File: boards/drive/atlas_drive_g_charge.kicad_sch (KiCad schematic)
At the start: 50 parts, among them J701 USB_C_16P, J702 EEPROM_PROG, U701 TPS25751D, U702 M24512, U703 BQ25798

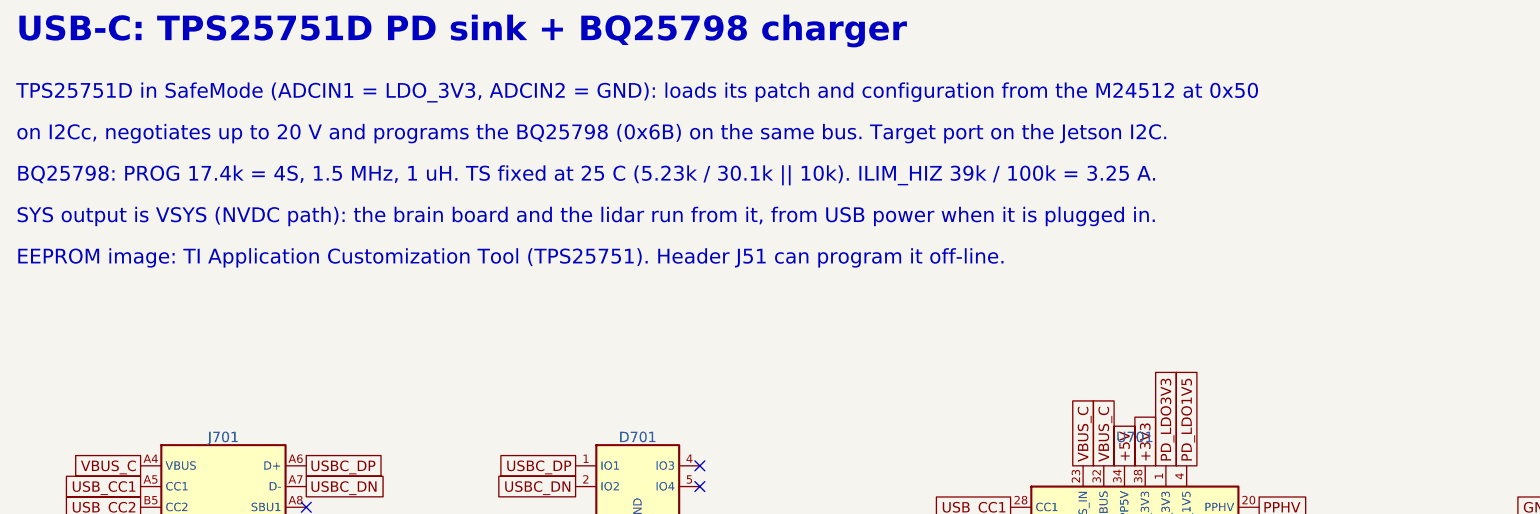
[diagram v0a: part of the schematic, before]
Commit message: Review fixes: docs, run_kicad.sh and drive board text
- README, docs/ARCHITECTURE.md, share/README.md, boards/tools/README.md: status,
  rebuild steps and tool notes brought up to date
- run_kicad.sh: the optional first argument is a sync tarball or an empty string
- Drive schematic text: header J702, 7.5 V servo rail, the precharge resistors
  take 0.15 J each (R319/R320 descriptions synced on the board)
- BOM wording: 7.5 V servo rail

DRC unchanged: no unconnected items, no clearance errors, 8 silkscreen and
track-end warnings.

Co-Authored-By: Claude Opus 5.5 <noreply@anthropic.com>
Claude-Session: https://claude.ai/code/session_01XVBHou86msuHYBGRPr641F
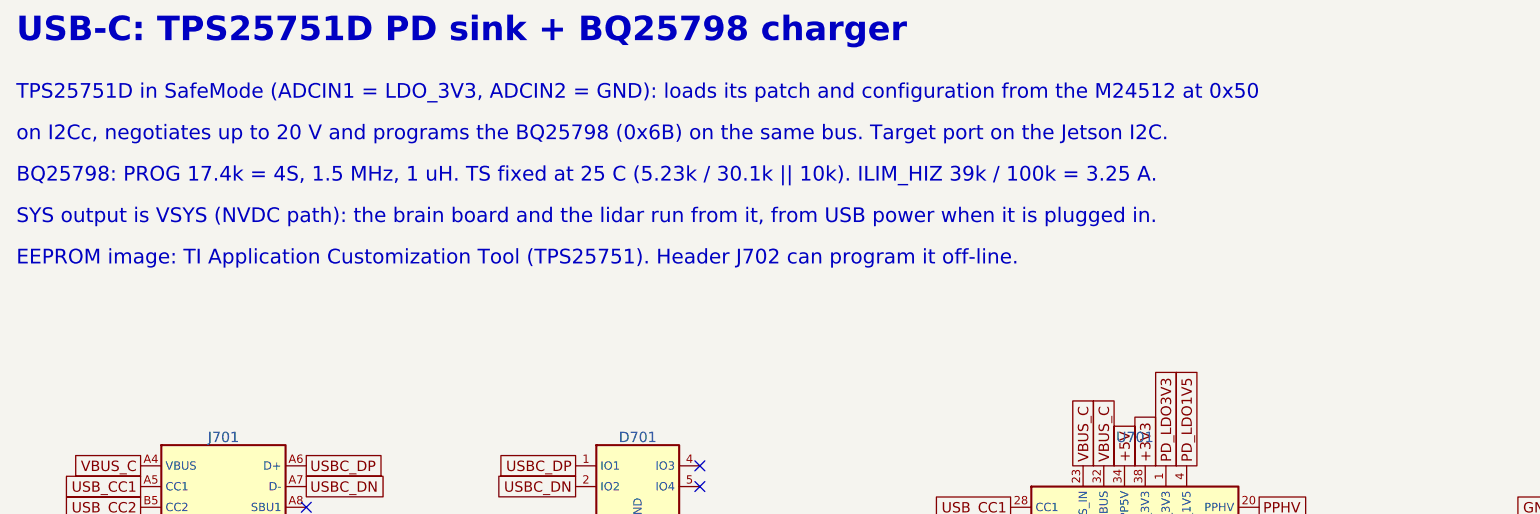
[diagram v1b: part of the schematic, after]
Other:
- note added: "EEPROM image: TI Application Customization Tool (TPS25751). Header J702 can program it off-line."
- note removed: "EEPROM image: TI Application Customization Tool (TPS25751). Header J51 can program it off-line."
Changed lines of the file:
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@@
 (text "BQ25798: PROG 17.4k = 4S, 1.5 MHz, 1 uH. TS fixed at 25 C (5.23k / 30.1k || 10k). ILIM_HIZ 39k / 100k = 3.25 A." (exclude_from_sim no) (at 25.4 43.18000000000001 0) (effects (font (size 1.8 1.8)) (justify left)))
 (text "SYS output is VSYS (NVDC path): the brain board and the lidar run from it, from USB power when it is plugged in." (exclude_from_sim no) (at 25.4 48.260000000000005 0) (effects (font (size 1.8 1.8)) (justify left)))
-(text "EEPROM image: TI Application Customization Tool (TPS25751). Header J51 can program it off-line." (exclude_from_sim no) (at 25.4 53.34 0) (effects (font (size 1.8 1.8)) (justify left)))
+(text "EEPROM image: TI Application Customization Tool (TPS25751). Header J702 can program it off-line." (exclude_from_sim no) (at 25.4 53.34 0) (effects (font (size 1.8 1.8)) (justify left)))
 (symbol (lib_id "atlas:USB_C_16P") (at 50.80 83.82 0) (unit 1) (exclude_from_sim no) (in_bom yes) (on_board yes) (dnp no)
  (property "Reference" "J701" (at 50.80 75.24 0) (effects (font (size 1.27 1.27)) )) (property "Value" "USB_C_16P" (at 50.80 97.48 0) (effects (font (size 1.27 1.27)) )) (property "Footprint" "Connector_USB:USB_C_Receptacle_GCT_USB4105-xx-A_16P_TopMnt_Horizontal" (at 50.80 83.82 0) (effects (font (size 1.27 1.27)) (hide yes))) (property "Datasheet" "" (at 50.80 83.82 0) (effects (font (size 1.27 1.27)) (hide yes))) (property "MPN" "USB4105-GF-A" (at 50.80 83.82 0) (effects (font (size 1.27 1.27)) (hide yes))) (property "Manufacturer" "GCT" (at 50.80 83.82 0) (effects (font (size 1.27 1.27)) (hide yes))) (property "Description" "USB-C receptacle, USB 2.0, 5 A VBUS" (at 50.80 83.82 0) (effects (font (size 1.27 1.27)) (hide yes))) (pin "A4") (pin "A9") (pin "B4") (pin "B9") (pin "A5") (pin "B5") (pin "A6") (pin "B6") (pin "A7") (pin "B7") (pin "A8") (pin "B8") (pin "A1") (pin "A12") (pin "B1") (pin "B12") (pin "SH")
